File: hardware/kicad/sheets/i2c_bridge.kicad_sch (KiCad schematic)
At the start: 11 parts, among them U25 SC18IS604PW, U26 74LVC1G125

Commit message: Move the IMU off-board (J14) and add labelled module boxes to the PCB
The LSM6DSOX is now the Adafruit breakout (product 4438) mounted on the
cryocooler and cabled to a 10-pin JST XH header (J14) over the shared SPI
bus. U19 and its capacitors are gone; J14 and six 100 R series resistors
are added, and every other reference number is unchanged.

PCB (130 x 110 mm, was 130 x 100):
- one outlined, labelled silkscreen box per module (pcbfloorplan.py); the
  placer keeps parts inside their box and reserves a label pocket beside
  every part so each label sits next to its own part
- box 3D models for U3, L2, L3, F1 and PS1, whose library models are missing
- re-routed; DRC 0 errors, 0 unconnected; back logo recentred
- gen_pcb.py texts redoes the silkscreen on a routed board

Firmware: SPI clock constant for the module, comments updated; ambient
temperature now reads the cooler-body IMU temperature.

Docs, BOM and fabrication files regenerated.

Co-Authored-By: Claude Sonnet 5.5 <noreply@anthropic.com>
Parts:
- removed C78: 1uF, Capacitor_SMD:C_0805_2012Metric, symbol Device:C
- removed R84: 4.7k, Resistor_SMD:R_0603_1608Metric, symbol Device:R_US
- added R81: 10k, Resistor_SMD:R_0603_1608Metric, symbol Device:R_US
- added U26: 74LVC1G125, Package_TO_SOT_SMD:SOT-23-5, symbol cryocooler:74LVC1G125
- C78: renamed from C79; value 100nF -> 1uF; footprint Capacitor_SMD:C_0603_1608Metric -> Capacitor_SMD:C_0805_2012Metric
- C79: renamed from R81; value 10k -> 100nF; footprint Resistor_SMD:R_0603_1608Metric -> Capacitor_SMD:C_0603_1608Metric; symbol Device:R_US -> Device:C
- R84: renamed from U26; value 74LVC1G125 -> 4.7k; footprint Package_TO_SOT_SMD:SOT-23-5 -> Resistor_SMD:R_0603_1608Metric; symbol cryocooler:74LVC1G125 -> Device:R_US
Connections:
- net +3V3: now also R84.1, R81.1, U26.5 (VCC); no longer R84.5 (VCC)
- net BRIDGE_CS: now also R81.2, U26.1; no longer C79.2, R84.1
- net GND: now also C79.2, U26.3 (GND); no longer R84.3 (GND)
- net SDA: now also R84.2
- net SPI_MISO: now also U26.4; no longer R84.4
- net at U25.14 (MISO): now also U26.2; no longer R84.2
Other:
- moved on the sheet: C78

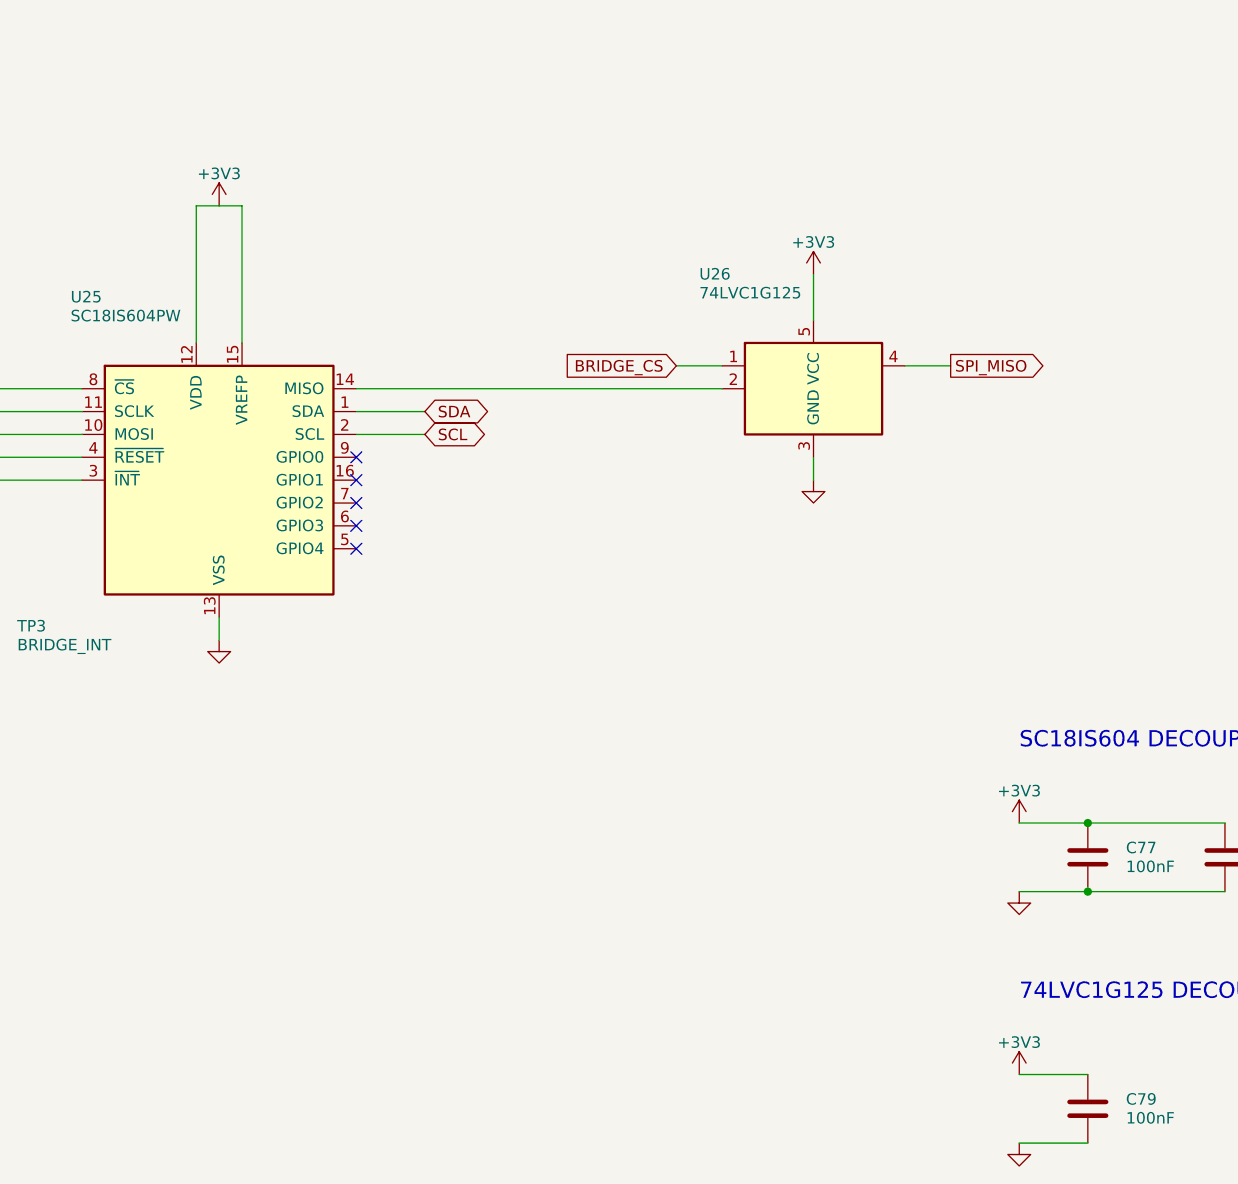
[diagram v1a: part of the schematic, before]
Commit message: Add per-section supply jumpers, 8-pin IMU header and connector pin labels
- Four 1.27 mm 2-pin jumpers (JP1-JP4), each with a rail-on LED, cut the
  supply of one section for debugging: signal generator +3V3, +-15V
  generator +5V in, isolated amp-current supply +5V in, and a shared
  +3V3 net for the cooling chips (EMC2303, RTD ADC, I2C bridge).
- J14 is now an 8-pin JST XH in the Adafruit LSM6DSOX pad order
  (VIN, GND, SCL, SDA, DO, CS, I1, I2); firmware pin comments updated.
- Pin-function labels beside every connector, "RAILS ±15V" box title.
- Board re-placed and re-routed (130 x 110 mm); DRC 0 errors, 0 unconnected,
  ERC 0, 173 datasheet rules pass. BOM, READMEs, Gerbers and renders
  regenerated; link_usb_vbus.py now adapts to the routed layout.

Co-Authored-By: Claude Sonnet 5.5 <noreply@anthropic.com>
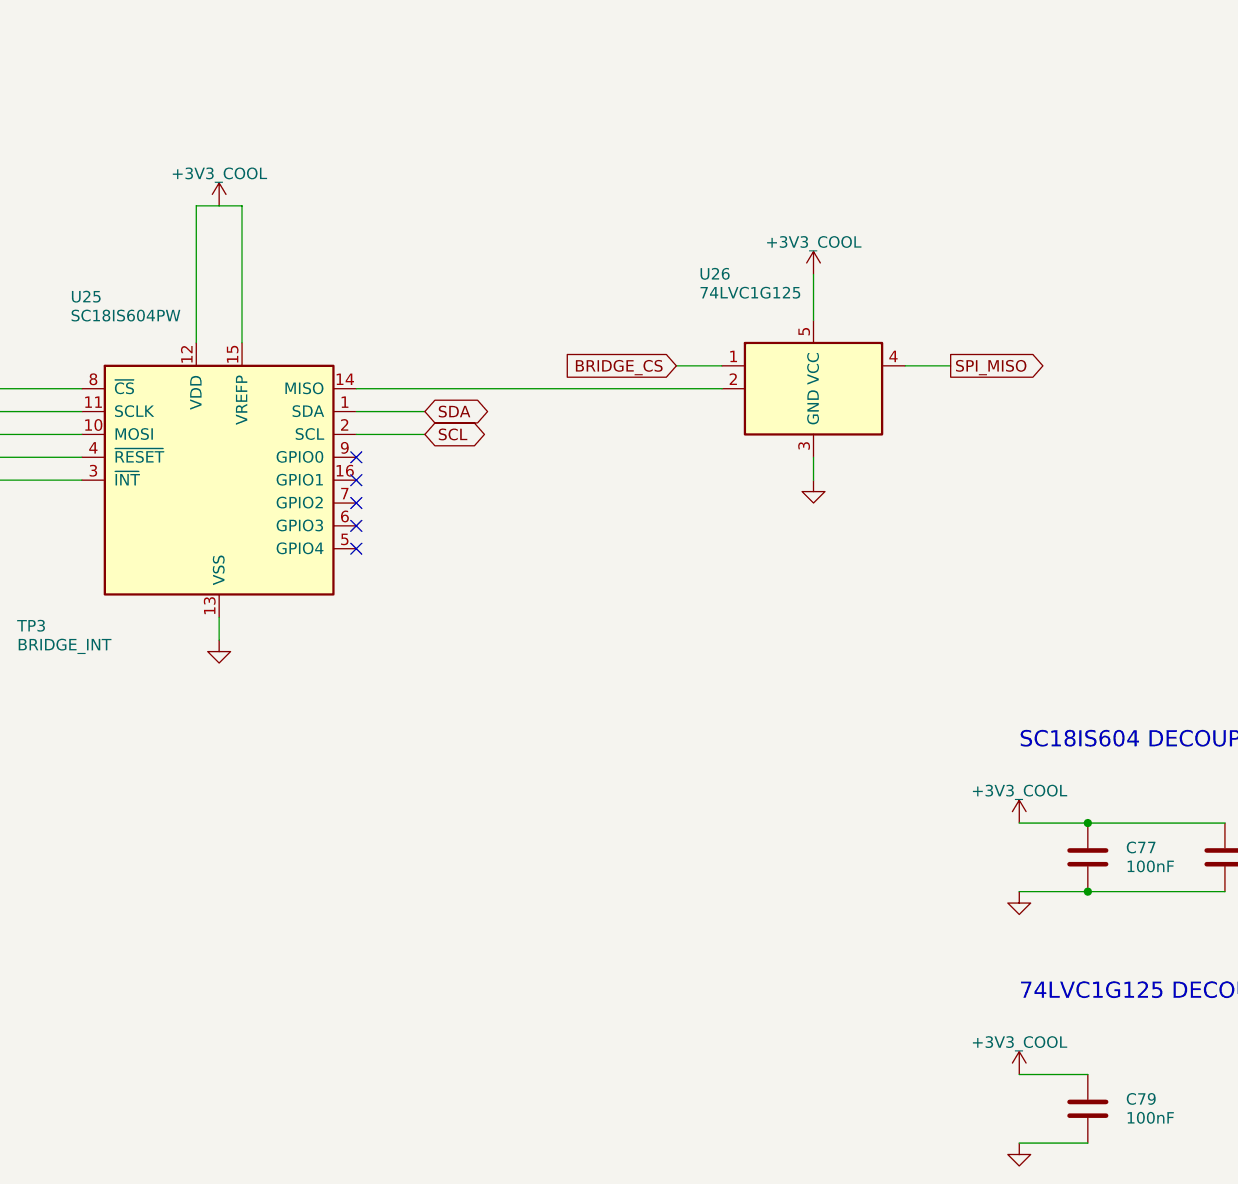
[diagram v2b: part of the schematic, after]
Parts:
- removed R85: 4.7k, Resistor_SMD:R_0603_1608Metric, symbol Device:R_US
- added TP3: BRIDGE_INT, TestPoint:TestPoint_Pad_D1.5mm, symbol Connector:TestPoint
- R81: renamed from TP3; value BRIDGE_INT -> 10k; footprint TestPoint:TestPoint_Pad_D1.5mm -> Resistor_SMD:R_0603_1608Metric; symbol Connector:TestPoint -> Device:R_US
- R84: renamed from R83; value 10k -> 4.7k
- renumbered R81 to R82, R82 to R83, R84 to R85
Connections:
- net +3V3: now also R81.1; no longer C77.1, C78.1, C79.1, U25.12 (VDD), U25.15 (VREFP), U26.5 (VCC)
- net BRIDGE_CS: now also R81.2; no longer R82.2
- net BRIDGE_INT: now also R83.2, TP3.1; no longer R81.1, R84.2
- net BRIDGE_RESET: now also R82.2; no longer R83.2
- net SCL: now also R85.2
- net SDA: now also R84.2; no longer R85.2
- new net +3V3_COOL: C77.1, C78.1, C79.1, U25.12 (VDD), U25.15 (VREFP), U26.5 (VCC)
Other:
- moved on the sheet: R82, R83, R84, R85

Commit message: Split cooling into Water Cooling and Cold Head Temp sections, each with a supply jumper and LED
Water Cooling (EMC2303, SC18IS604 bridge, NTC, fan/pump/flow) sits behind JP4
on +3V3_COOL together with its pull-ups. Cold Head Temp (ADS1220, PT1000) gets
a new jumper JP5 and LED D22 on +3V3_CH. JP2 is relabelled for the +-15V rails
and moved into the RAILS +-15V box. PCB regenerated with two silk boxes, routed,
leftovers finished with a grid router; board render added to the main README.

Co-Authored-By: Claude Sonnet 5.5 <noreply@anthropic.com>
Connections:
- net +3V3: no longer R83.1, R84.1, R85.1
- net +3V3_COOL: now also R83.1, R84.1, R85.1
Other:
- title: I2C Bridge -> Water Cooling I2C Bridge

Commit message: Replace the ±15 V LDOs with one LT3097 and add a power-good interlock
- rails_15v: ADP7142 + ADP7182 replaced by one LT3097 (±14.7 V, 147 k SET
  resistors); the ADP5071 output caps are now 22 uF / 50 V and double as the
  LT3097 inputs. PGP / PGN make the PG_15V node (fed from +15 V, so it reads
  0 V if a rail is missing).
- amp_control: a series BSS138 (Q9) gated by PG_15V blocks AMP_REM unless
  both rails are good. New power_good sheet: LED (D23) and the active-low
  PG_15V_N flag on GPIO43 (PG_15V_N_PIN).
- Tooling: LT3097 symbol, footprint and 3D envelope; datasheet rules (191),
  GPIO check, BOM tables, floor plan, PAD_BRIDGES and pre-placed GND vias in
  gen_pcb.py, new fix_route.py for post-route clean-up.
- Board regenerated and routed with Freerouting 2.5.0: DRC 0 unconnected,
  0 schematic-parity issues, no copper violations. Gerbers, JLCPCB zip,
  renders, BOM, CPL and schematic PDF regenerated.

Co-Authored-By: Claude Sonnet 5.5 <noreply@anthropic.com>
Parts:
- removed C77: 100nF, Capacitor_SMD:C_0603_1608Metric, symbol Device:C
- added R84: 4.7k, Resistor_SMD:R_0603_1608Metric, symbol Device:R_US
- C77: renamed from R84; value 4.7k -> 100nF; footprint Resistor_SMD:R_0603_1608Metric -> Capacitor_SMD:C_0603_1608Metric; symbol Device:R_US -> Device:C
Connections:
- net +3V3_COOL: now also R84.1
- net GND: now also C77.2
- net SDA: now also R84.2; no longer C77.2

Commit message: Log +-15 V power-good changes and add one LED per LT3097 PG pin
Firmware
- amplifier: configure PG_15V_N_PIN (GPIO43, active LOW), log the starting
  state and every debounced change (PowerGoodMonitor in power_good.h);
  amplifier::isPowerGood() reports the level. The lines reach the dashboard
  console through the logger ring buffer.
- dashboard: console colours for "power lost" (red), "power restored" and
  "power good: yes" (green), "power good: no" (yellow).
- native tests for the debounce logic and the amplifier stub.

Hardware
- power_good sheet: PGP and PGN each drive their own node (220k/62k from
  +15 V) and a green LED (D24 +15 V, D25 -15 V) through a BSS138W; a BAT54AW
  with a 10k pull-up ANDs the nodes into PG_15V, so the REM interlock and the
  PG_15V_N flag are unchanged.
- 0402 resistors, SOT-323 FETs and one BAT54AW so the stage fits the power
  box; Power Good parts are placed last in gen_pcb.py.
- Board re-routed with Freerouting 2.5.0 and cleaned with fix_route.py: DRC
  0 unconnected, no copper violations. Gerbers, JLCPCB zip, renders, BOM, CPL
  and schematic PDF regenerated; datasheet rules 193/193.

Co-Authored-By: Claude Sonnet 5.5 <noreply@anthropic.com>
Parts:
- removed C77: 100nF, Capacitor_SMD:C_0603_1608Metric, symbol Device:C
- removed C78: 1uF, Capacitor_SMD:C_0805_2012Metric, symbol Device:C
- added R85: 4.7k, Resistor_SMD:R_0603_1608Metric, symbol Device:R_US
- added U26: 74LVC1G125, Package_TO_SOT_SMD:SOT-23-5, symbol cryocooler:74LVC1G125
- C77: renamed from R85; value 4.7k -> 100nF; footprint Resistor_SMD:R_0603_1608Metric -> Capacitor_SMD:C_0603_1608Metric; symbol Device:R_US -> Device:C
- C78: renamed from U26; value 74LVC1G125 -> 1uF; footprint Package_TO_SOT_SMD:SOT-23-5 -> Capacitor_SMD:C_0805_2012Metric; symbol cryocooler:74LVC1G125 -> Device:C
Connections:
- net +3V3_COOL: now also C78.1, R85.1, U26.5 (VCC); no longer C78.5 (VCC)
- net BRIDGE_CS: now also U26.1; no longer C78.1
- net GND: now also C77.2, C78.2, U26.3 (GND); no longer C78.3 (GND)
- net SCL: now also R85.2; no longer C77.2
- net SPI_MISO: now also U26.4; no longer C78.4
- net at U25.14 (MISO): now also U26.2; no longer C78.2

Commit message: WIP: restructure PCB for the Phoenix UCS 125-87 housing
Work in progress, layout not finished: about 90 parts still do not fit
their sections and the board is not routed.

- Right-angle connectors: Phoenix MSTBA 2,5 / MC 1,5, JST XH side entry,
  Hirose DF13, Molex 505448-0871 (new footprint from the Molex drawing)
- Datasheet and product links on every symbol (tools/part_links.py)
- Test points so every IC has one on its own nets
- gen_pcb.py: 100 x 62 mm two-sided board, housing holes and restricted
  corners, ESP32 antenna notch, one section per sheet, board ID block,
  ESP32 pin names, pin-1 marks, blue mask
- Housing drawings in hardware/housing/

Co-Authored-By: Claude Opus 5.5 <noreply@anthropic.com>
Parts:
- removed C78: 1uF, Capacitor_SMD:C_0805_2012Metric, symbol Device:C
- removed R84: 4.7k, Resistor_SMD:R_0603_1608Metric, symbol Device:R_US
- removed TP3: BRIDGE_INT, TestPoint:TestPoint_Pad_D1.5mm, symbol Connector:TestPoint
- added R81: 10k, Resistor_SMD:R_0603_1608Metric, symbol Device:R_US
- added TP6: BRIDGE_INT, TestPoint:TestPoint_Pad_D1.5mm, symbol Connector:TestPoint
- added U26: 74LVC1G125, Package_TO_SOT_SMD:SOT-23-5, symbol cryocooler:74LVC1G125
- C77: Product (none) -> https://www.digikey.com/en/products/result?keywords=C0603C1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
- C78: renamed from C79; value 100nF -> 1uF; footprint Capacitor_SMD:C_0603_1608Metric -> Capacitor_SMD:C_0805_2012Metric; Product (none) -> https://www.digikey.com/en/products/result?keywords=08055C1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
- C79: renamed from R81; value 10k -> 100nF; footprint Resistor_SMD:R_0603_1608Metric -> Capacitor_SMD:C_0603_1608Metric; symbol Device:R_US -> Device:C; Product (none) -> https://www.digikey.com/en/products/result?keywords=C0603C1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
- R82, R83: Product (none) -> https://www.digikey.com/en/products/result?keywords=AR0603F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
- R84: renamed from U26; value 74LVC1G125 -> 4.7k; footprint Package_TO_SOT_SMD:SOT-23-5 -> Resistor_SMD:R_0603_1608Metric; symbol cryocooler:74LVC1G125 -> Device:R_US; Product (none) -> https://www.digikey.com/en/products/result?keywords=RC0603F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
- R85: Product (none) -> https://www.digikey.com/en/products/result?keywords=RC0603F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
- U25: Product (none) -> https://www.digikey.com/en/products/result?keywords=SC18IS6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
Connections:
- net +3V3: now also R81.1; no longer C79.1
- net +3V3_COOL: now also C79.1, R84.1, U26.5 (VCC); no longer R84.5 (VCC)
- net BRIDGE_CS: now also R81.2, U26.1; no longer C79.2, R84.1
- net BRIDGE_INT: now also TP6.1
- net GND: now also C79.2, U26.3 (GND); no longer R84.3 (GND)
- net SDA: now also R84.2
- net SPI_MISO: now also U26.4; no longer R84.4
- net at U25.14 (MISO): now also U26.2; no longer R84.2
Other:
- moved on the sheet: C78

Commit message: Lay out the board for the Phoenix UCS 145-125 housing
Move to a 120 x 100 mm, 4-layer, blue-mask board for the UCS 145-125-F-CCD
7035 housing: housing mounting holes and restricted corners, ESP32 antenna
over a routed notch, one labelled section per schematic sheet with almost
every part on top. Placed, routed and cleaned up: DRC 0 errors, 0
unconnected, 0 schematic-parity issues; ERC 0; 193/193 datasheet rules.

- AGENTS.md: test points go on the same side as the part they test, close
  to it
- gen_pcb: test points held to their IC's side and within 8 mm; silkscreen
  check measures text by ink and also fails on pads, part outlines, section
  lines and pin-1 dots; titles along or up a border; connector labels and
  ESP32 pin names reserved before the passives; pin-1 dots only where the
  footprint has no mark; footprints carry the schematic's library links and
  fields; mounting holes are board-only H1-H4
- fix_route: generic clean-up (no old-board coordinate edits); removes GND
  vias in keep-outs or on foreign pads, links stranded ground pads, nudges
  squeezed tracks, handles back-side pour islands
- kicad_dru: fix the rule file (an invalid USB-C rule made KiCad ignore it);
  housing-corner and antenna keep-out part rules
- schematic: pad test points excluded from the BOM
- README / fabrication README updated for the new board

Co-Authored-By: Claude Opus 5.5 <noreply@anthropic.com>
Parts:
- TP6: now left out of the parts list
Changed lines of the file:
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@@
 		(body_style 1)
 		(exclude_from_sim no)
-		(in_bom yes)
+		(in_bom no)
 		(on_board yes)
 		(in_pos_files yes)

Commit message: Ground the M12 shield, order the ground loops, name the J14 cable parts
- J10: shielded symbol (Conn_01x04_Shielded); the M12 shield pin and its
  four shell legs are pad SH, tied to GND
- TP22-TP25: Keystone 5001 black miniature PC test points (KiCad
  TestPoint_Keystone_5000-5004 footprint, 1.02 mm hole per Keystone's
  drawing); now in the BOM, the bare pad test points stay out
- J14 BOM note: cable housing Molex 5054320801 with 505431 terminals, or
  tin pre-crimped leads 797581148 / 797581149 (from molex.com)

Only netlist change: GND gains J10 SH. DRC 0 errors, 0 unconnected, 0
schematic-parity issues; ERC 0; 193/193 datasheet rules.

Co-Authored-By: Claude Opus 5.5 <noreply@anthropic.com>
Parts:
- removed C77, C79: 100nF, Capacitor_SMD:C_0603_1608Metric, symbol Device:C
- removed R85: 4.7k, Resistor_SMD:R_0603_1608Metric, symbol Device:R_US
- added C78: 1uF, Capacitor_SMD:C_0805_2012Metric, symbol Device:C
- added TP6: BRIDGE_INT, TestPoint:TestPoint_Pad_D1.5mm, symbol Connector:TestPoint
- added U26: 74LVC1G125, Package_TO_SOT_SMD:SOT-23-5, symbol cryocooler:74LVC1G125
- C77: renamed from C78; value 1uF -> 100nF; footprint Capacitor_SMD:C_0805_2012Metric -> Capacitor_SMD:C_0603_1608Metric; Product https://www.digikey.com/en/products/result?keywords=08055C1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 -> https://www.digikey.com/en/products/result?keywords=C0603C1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
- C79: renamed from TP6; value BRIDGE_INT -> 100nF; footprint TestPoint:TestPoint_Pad_D1.5mm -> Capacitor_SMD:C_0603_1608Metric; symbol Connector:TestPoint -> Device:C; Product (none) -> https://www.digikey.com/en/products/result?keywords=C0603C1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; now in the parts list
- R85: renamed from U26; value 74LVC1G125 -> 4.7k; footprint Package_TO_SOT_SMD:SOT-23-5 -> Resistor_SMD:R_0603_1608Metric; symbol cryocooler:74LVC1G125 -> Device:R_US; Product https://www.digikey.com/en/products/result?keywords=74LVC1G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 -> https://www.digikey.com/en/products/result?keywords=RC0603F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
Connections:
- net +3V3_COOL: now also C79.1, R85.1, C78.1, U26.5 (VCC); no longer R85.5 (VCC)
- net BRIDGE_CS: now also U26.1; no longer R85.1
- net BRIDGE_INT: now also TP6.1; no longer C79.1
- net GND: now also C79.2, C78.2, U26.3 (GND); no longer R85.3 (GND)
- net SCL: now also R85.2
- net SPI_MISO: now also U26.4; no longer R85.4
- net at U25.14 (MISO): now also U26.2; no longer R85.2
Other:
- moved on the sheet: C77
